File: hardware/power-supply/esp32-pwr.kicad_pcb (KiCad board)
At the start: 4 copper layers, 25 x 40 mm, 11 parts, among them P101 EXT_HEADER, P102 PWR IN, P103 EXT_HEADER, U101 WPMDL110

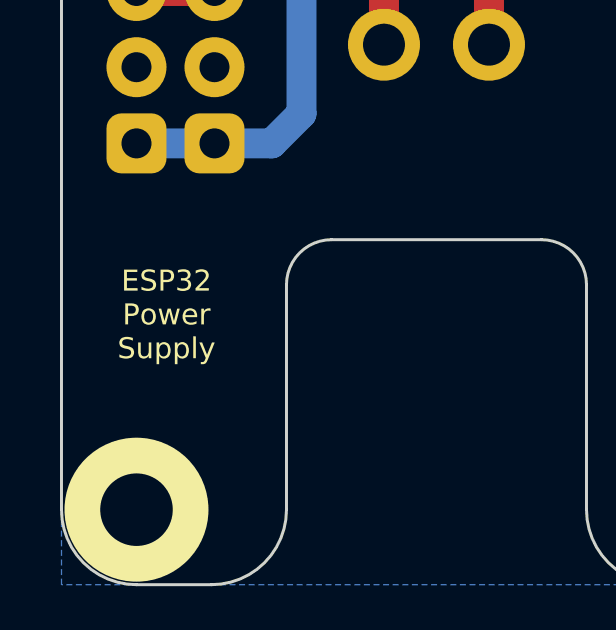
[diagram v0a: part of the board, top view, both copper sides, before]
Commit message: switch from 4 layer design to 2 layer
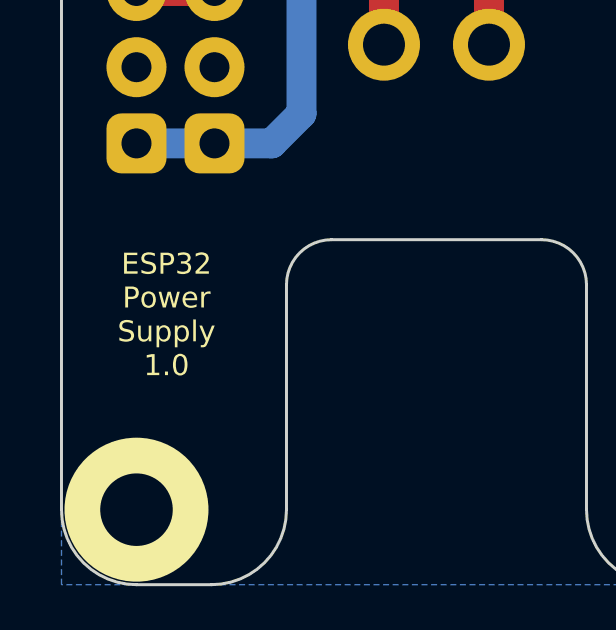
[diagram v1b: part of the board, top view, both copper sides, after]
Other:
- copper layers 4 -> 2
- board text added: "ESP32 Power Supply 1.0"
- board text removed: "ESP32 Power Supply"
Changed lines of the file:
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@@
   (layers
     (0 F.Cu signal)
-    (1 GND power hide)
-    (2 VCC power hide)
-    (31 B.Cu signal hide)
+    (31 B.Cu signal)
     (32 B.Adhes user)
     (33 F.Adhes user)
@@
   )
   (setup
-    (last_trace_width 1)
+    (last_trace_width 0.15)
     (user_trace_width 0.15)
     (user_trace_width 0.2)
@@
     (effects (font (size 1.524 1.524) (thickness 0.3048)))
   )
-  (gr_text "ESP32\nPower\nSupply" (at 152.3 154.65) (layer F.SilkS)
+  (gr_text "ESP32\nPower\nSupply\n1.0" (at 152.3 154.65) (layer F.SilkS)
     (effects (font (size 0.7 0.7) (thickness 0.15)))
   )

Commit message: updated footprints drc
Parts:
- moved VAL 8.53 mm to (162.8, 140.4)
- moved VAL 7.75 mm to (162.8, 129.8)
- moved U101 4.27 mm to (162.8, 136.3), turned to 180 degrees
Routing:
- net GND: track 14.0 -> 9.40 mm
- net Net-(P102-Pad1): track 13.6 -> 9.71 mm
- net 5V: track 24.4 -> 22.6 mm

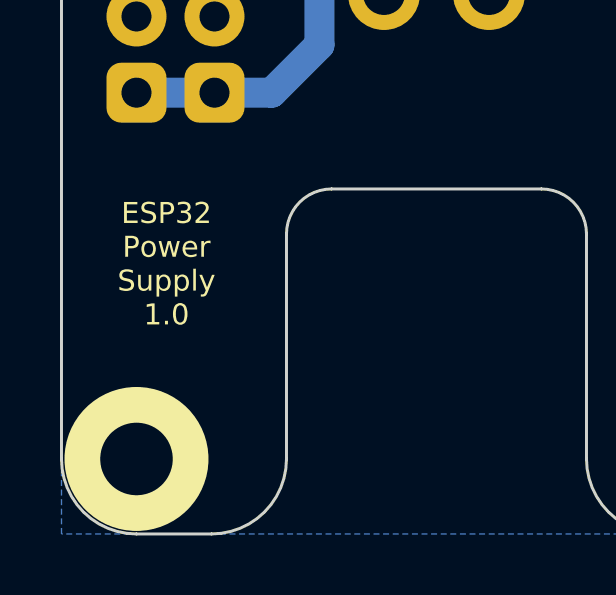
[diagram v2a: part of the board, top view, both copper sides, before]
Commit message: changed version number on silkscreen
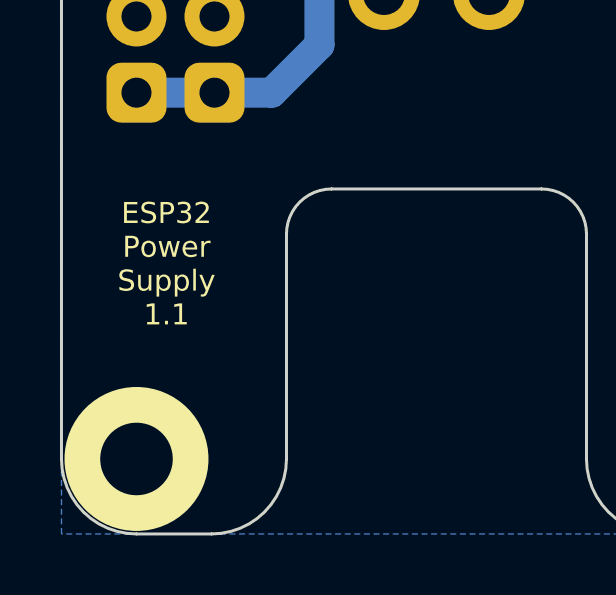
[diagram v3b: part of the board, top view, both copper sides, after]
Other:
- board text added: "ESP32 Power Supply 1.1"
- board text removed: "ESP32 Power Supply 1.0"
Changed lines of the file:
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@@
     (title "ESP32 Brick Power Supply")
     (date 2020-08-05)
-    (rev 1.0)
+    (rev 1.1)
     (company "Tinkerforge GmbH")
     (comment 1 "Licensed under CERN OHL v.1.1")
@@
       (drillshape 0)
       (scaleselection 1)
-      (outputdirectory "../../../../Schreibtisch/proto/ESP_Power_Supply/"))
+      (outputdirectory "../../../../Schreibtisch/proto/powerESP/"))
   )
   (net 0 "")
@@
     (effects (font (size 1.524 1.524) (thickness 0.3048)))
   )
-  (gr_text "ESP32\nPower\nSupply\n1.0" (at 152.3 154.65) (layer F.SilkS)
+  (gr_text "ESP32\nPower\nSupply\n1.1" (at 152.3 154.65) (layer F.SilkS)
     (effects (font (size 0.7 0.7) (thickness 0.15)))
   )

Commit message: update
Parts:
- U101: value WPMDL110 -> WPMDL1100501S
